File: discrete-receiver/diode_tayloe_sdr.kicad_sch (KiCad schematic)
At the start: 9 parts, among them J5 Display Connector, X1 YC24.576MUBCE2O

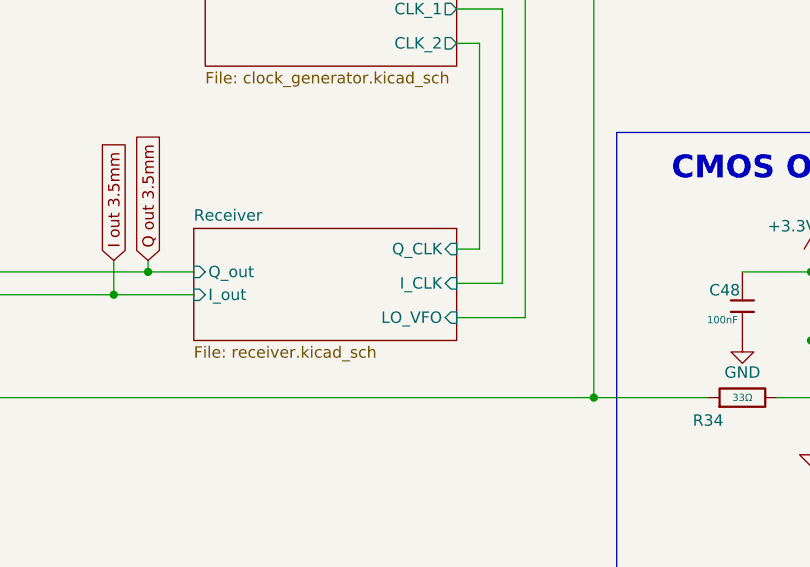
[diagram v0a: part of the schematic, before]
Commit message: Modified I, Q, and IF_LO clock order from si5351
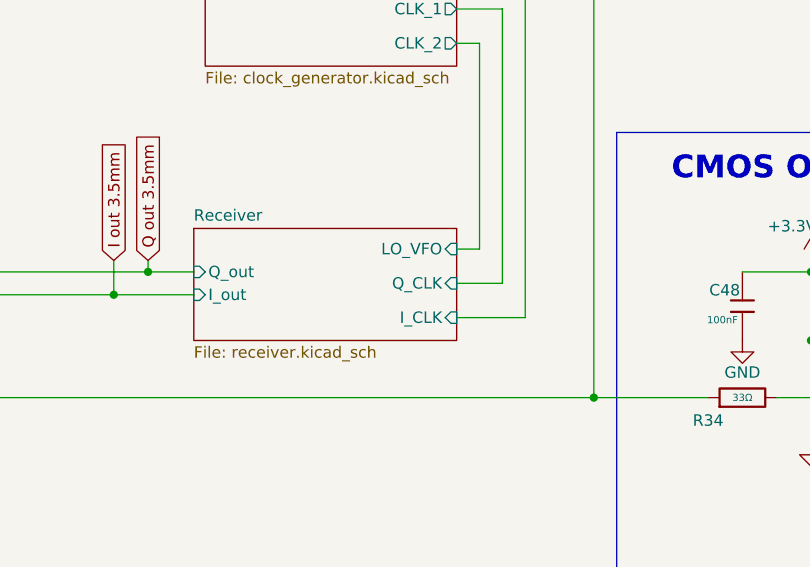
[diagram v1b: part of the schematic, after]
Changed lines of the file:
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@@
 	(wire
 		(pts
-			(xy 224.79 132.08) (xy 219.71 132.08)
+			(xy 222.25 105.41) (xy 222.25 128.27)
 		)
 		(stroke
@@
 	(wire
 		(pts
-			(xy 166.37 133.35) (xy 181.61 133.35)
+			(xy 224.79 132.08) (xy 219.71 132.08)
 		)
 		(stroke
@@
 	(wire
 		(pts
-			(xy 45.72 53.34) (xy 45.72 54.61)
+			(xy 166.37 133.35) (xy 181.61 133.35)
 		)
 		(stroke
@@
 	(wire
 		(pts
-			(xy 120.65 54.61) (xy 133.35 54.61)
+			(xy 45.72 53.34) (xy 45.72 54.61)
 		)
 		(stroke
@@
 	(wire
 		(pts
-			(xy 227.33 135.89) (xy 219.71 135.89)
+			(xy 120.65 54.61) (xy 133.35 54.61)
 		)
 		(stroke
@@
 	(wire
 		(pts
-			(xy 224.79 101.6) (xy 224.79 132.08)
-		)
-		(stroke
-			(width 0)
-			(type default)
-		)
-	)
-	(wire
-		(pts
 			(xy 259.08 130.81) (xy 259.08 138.43)
 		)
@@
 	(wire
 		(pts
-			(xy 222.25 128.27) (xy 219.71 128.27)
+			(xy 227.33 97.79) (xy 227.33 135.89)
 		)
 		(stroke
@@
 	(wire
 		(pts
-			(xy 227.33 97.79) (xy 227.33 135.89)
+			(xy 45.72 46.99) (xy 45.72 48.26)
 		)
 		(stroke
@@
 	(wire
 		(pts
-			(xy 45.72 46.99) (xy 45.72 48.26)
+			(xy 120.65 57.15) (xy 133.35 57.15)
 		)
 		(stroke
@@
 	(wire
 		(pts
-			(xy 120.65 57.15) (xy 133.35 57.15)
+			(xy 274.32 138.43) (xy 259.08 138.43)
 		)
 		(stroke
@@
 	(wire
 		(pts
-			(xy 274.32 138.43) (xy 259.08 138.43)
+			(xy 259.08 148.59) (xy 259.08 149.86)
 		)
 		(stroke
@@
 	(wire
 		(pts
-			(xy 259.08 148.59) (xy 259.08 149.86)
+			(xy 33.02 96.52) (xy 34.29 96.52)
 		)
 		(stroke
@@
 	(wire
 		(pts
-			(xy 33.02 96.52) (xy 34.29 96.52)
+			(xy 123.19 105.41) (xy 123.19 137.16)
 		)
 		(stroke
@@
 	(wire
 		(pts
-			(xy 123.19 105.41) (xy 123.19 137.16)
+			(xy 227.33 135.89) (xy 219.71 135.89)
 		)
 		(stroke
@@
 	(wire
 		(pts
-			(xy 166.37 130.81) (xy 185.42 130.81)
+			(xy 224.79 101.6) (xy 224.79 132.08)
 		)
 		(stroke
@@
 	(wire
 		(pts
-			(xy 33.02 69.85) (xy 33.02 72.39)
+			(xy 166.37 130.81) (xy 185.42 130.81)
 		)
 		(stroke
@@
 	(wire
 		(pts
-			(xy 222.25 105.41) (xy 222.25 128.27)
+			(xy 33.02 69.85) (xy 33.02 72.39)
 		)
 		(stroke
@@
 	(wire
 		(pts
+			(xy 222.25 128.27) (xy 219.71 128.27)
+		)
+		(stroke
+			(width 0)
+			(type default)
+		)
+	)
+	(wire
+		(pts
 			(xy 219.71 91.44) (xy 234.95 91.44)
 		)
@@
 		)
 		(pin "I_CLK" input
-			(at 219.71 132.08 0)
+			(at 219.71 135.89 0)
 			(effects
 				(font
@@
 		)
 		(pin "LO_VFO" input
-			(at 219.71 135.89 0)
+			(at 219.71 128.27 0)
 			(effects
 				(font
@@
 		)
 		(pin "Q_CLK" input
-			(at 219.71 128.27 0)
+			(at 219.71 132.08 0)
 			(effects
 				(font

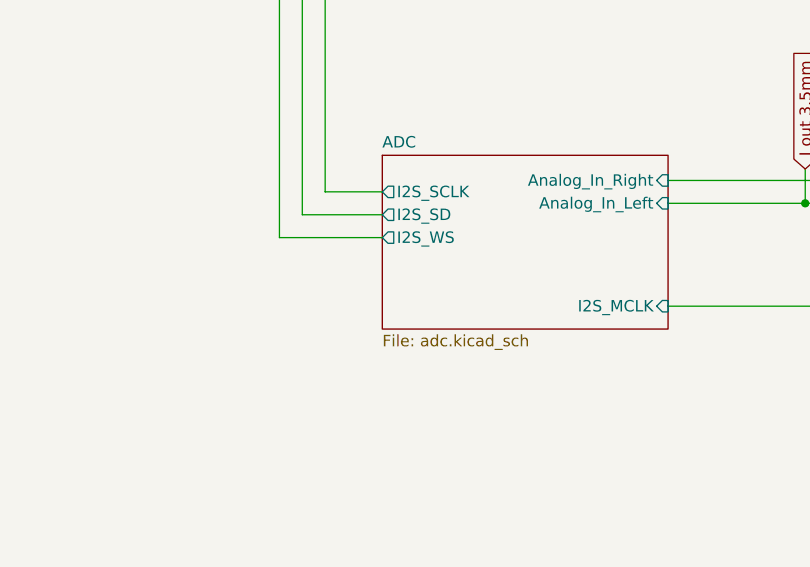
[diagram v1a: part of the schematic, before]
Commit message: Added ADC mode GPIO connections, and changed second red LED to green
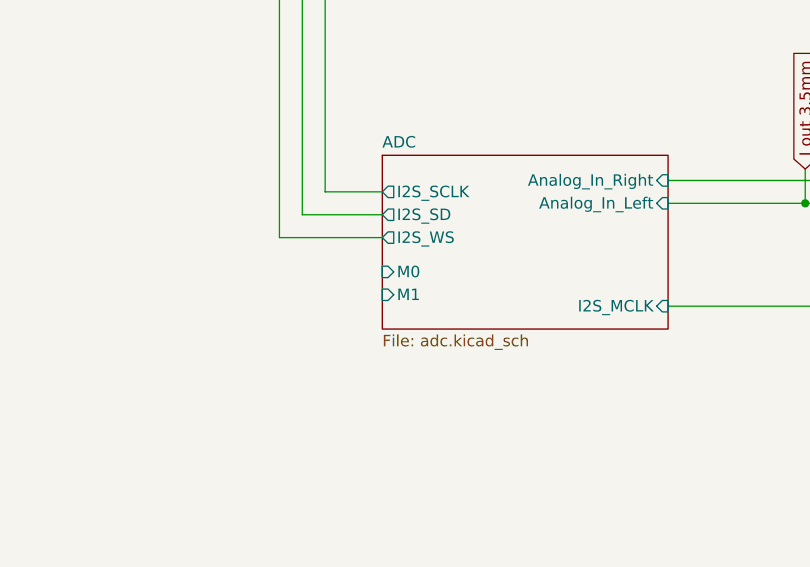
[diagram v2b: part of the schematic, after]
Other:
- sheet ADC ports: added M0, M1; removed none
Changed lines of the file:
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@@
+			)
+		)
+		(pin "M0" input
+			(at 134.62 140.97 180)
+			(effects
+				(font
+					(size 1.27 1.27)
+				)
+				(justify left)
+			)
+		)
+		(pin "M1" input
+			(at 134.62 143.51 180)
+			(effects
+				(font
+					(size 1.27 1.27)
+				)
+				(justify left)
 			)
 		)

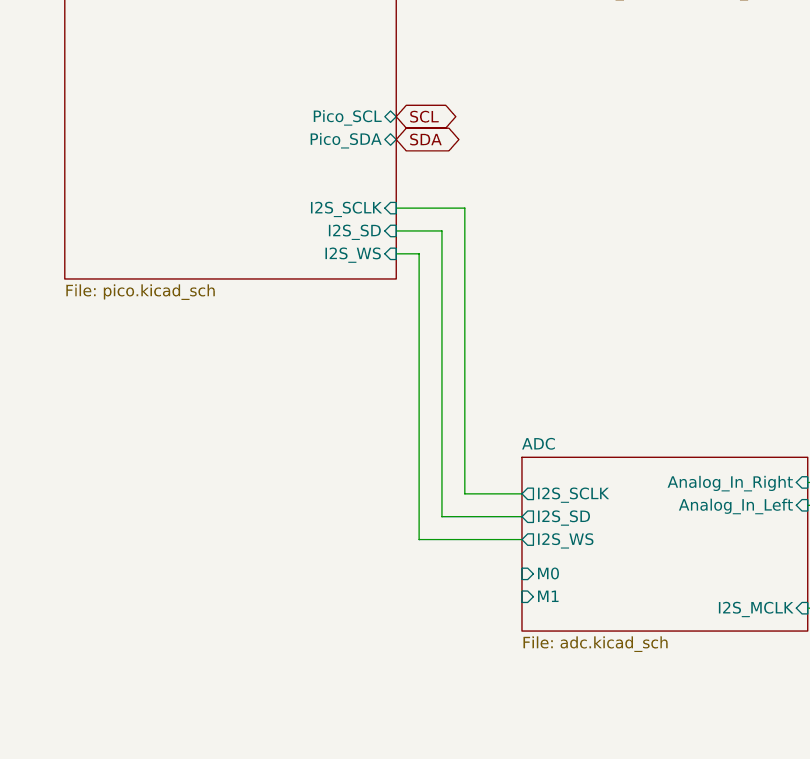
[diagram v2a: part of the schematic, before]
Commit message: Finished connecting ADC M0, M1, started PCB edge cut design
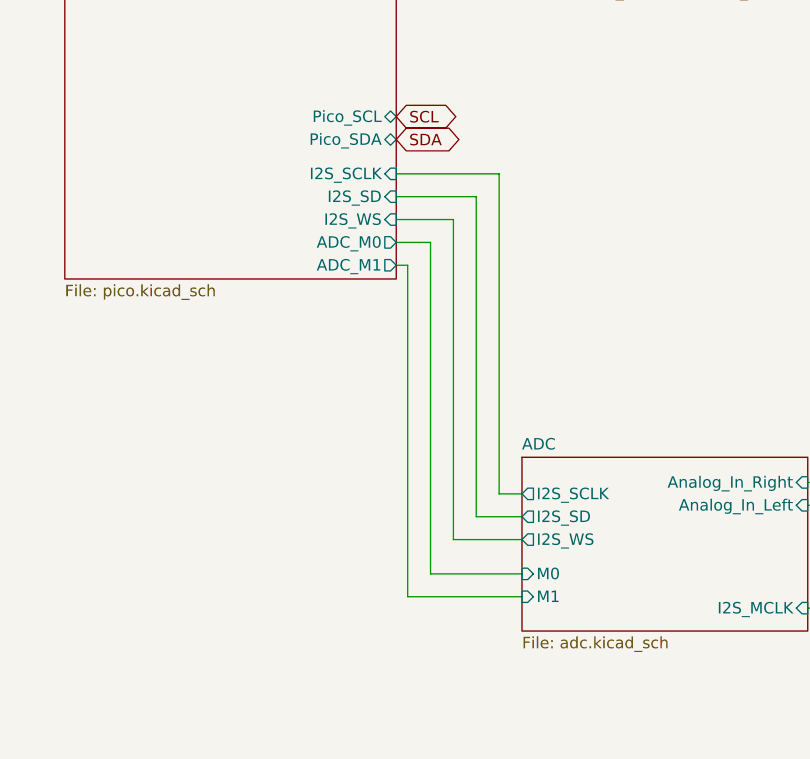
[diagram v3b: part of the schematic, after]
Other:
- sheet Pico ports: added ADC_M0, ADC_M1; removed none
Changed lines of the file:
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@@
 	(wire
 		(pts
+			(xy 120.65 104.14) (xy 124.46 104.14)
+		)
+		(stroke
+			(width 0)
+			(type default)
+		)
+	)
+	(wire
+		(pts
 			(xy 120.65 62.23) (xy 133.35 62.23)
 		)
@@
 	(wire
 		(pts
+			(xy 124.46 140.97) (xy 134.62 140.97)
+		)
+		(stroke
+			(width 0)
+			(type default)
+		)
+	)
+	(wire
+		(pts
 			(xy 166.37 133.35) (xy 181.61 133.35)
 		)
@@
 	(wire
 		(pts
-			(xy 123.19 137.16) (xy 134.62 137.16)
+			(xy 121.92 143.51) (xy 121.92 106.68)
+		)
+		(stroke
+			(width 0)
+			(type default)
+		)
+	)
+	(wire
+		(pts
+			(xy 127 137.16) (xy 134.62 137.16)
 		)
 		(stroke
@@
 	(wire
 		(pts
-			(xy 120.65 105.41) (xy 123.19 105.41)
+			(xy 120.65 101.6) (xy 127 101.6)
 		)
 		(stroke
@@
 	(wire
 		(pts
+			(xy 124.46 104.14) (xy 124.46 140.97)
+		)
+		(stroke
+			(width 0)
+			(type default)
+		)
+	)
+	(wire
+		(pts
 			(xy 55.88 39.37) (xy 59.69 39.37)
 		)
@@
 	(wire
 		(pts
+			(xy 121.92 106.68) (xy 120.65 106.68)
+		)
+		(stroke
+			(width 0)
+			(type default)
+		)
+	)
+	(wire
+		(pts
+			(xy 134.62 143.51) (xy 121.92 143.51)
+		)
+		(stroke
+			(width 0)
+			(type default)
+		)
+	)
+	(wire
+		(pts
 			(xy 259.08 138.43) (xy 259.08 140.97)
 		)
@@
 	(wire
 		(pts
-			(xy 123.19 105.41) (xy 123.19 137.16)
+			(xy 127 101.6) (xy 127 137.16)
 		)
 		(stroke
@@
 	(wire
 		(pts
-			(xy 120.65 100.33) (xy 128.27 100.33)
+			(xy 120.65 96.52) (xy 132.08 96.52)
 		)
 		(stroke
@@
 	(wire
 		(pts
-			(xy 125.73 134.62) (xy 134.62 134.62)
+			(xy 129.54 134.62) (xy 134.62 134.62)
 		)
 		(stroke
@@
 	(wire
 		(pts
-			(xy 128.27 132.08) (xy 134.62 132.08)
+			(xy 132.08 132.08) (xy 134.62 132.08)
 		)
 		(stroke
@@
 	(wire
 		(pts
-			(xy 125.73 102.87) (xy 125.73 134.62)
+			(xy 129.54 99.06) (xy 129.54 134.62)
 		)
 		(stroke
@@
 	(wire
 		(pts
-			(xy 128.27 100.33) (xy 128.27 132.08)
+			(xy 132.08 96.52) (xy 132.08 132.08)
 		)
 		(stroke
@@
 	(wire
 		(pts
-			(xy 120.65 102.87) (xy 125.73 102.87)
+			(xy 120.65 99.06) (xy 129.54 99.06)
 		)
 		(stroke
@@
 		)
 		(pin "I2S_SCLK" input
-			(at 120.65 100.33 0)
+			(at 120.65 96.52 0)
 			(effects
 				(font
@@
 		)
 		(pin "I2S_SD" input
-			(at 120.65 102.87 0)
+			(at 120.65 99.06 0)
 			(effects
 				(font
@@
 		)
 		(pin "I2S_WS" input
-			(at 120.65 105.41 0)
+			(at 120.65 101.6 0)
 			(effects
 				(font
@@
 			(effects
 				(font
+					(size 1.27 1.27)
+				)
+				(justify right)
+			)
+		)
+		(pin "ADC_M0" output
+			(at 120.65 104.14 0)
+			(effects
+				(font
+					(size 1.27 1.27)
+				)
+				(justify right)
+			)
+		)
+		(pin "ADC_M1" output
+			(at 120.65 106.68 0)
+			(effects
+				(font

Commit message: Made ERC progress
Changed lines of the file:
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@@
 	)
 	(junction
-		(at 45.72 53.34)
+		(at 181.61 133.35)
 		(diameter 0)
 		(color 0 0 0 0)
 	)
 	(junction
-		(at 55.88 39.37)
+		(at 45.72 53.34)
 		(diameter 0)
 		(color 0 0 0 0)
 	)
 	(junction
-		(at 33.02 72.39)
+		(at 55.88 39.37)
 		(diameter 0)
 		(color 0 0 0 0)
 	)
 	(junction
-		(at 234.95 144.78)
+		(at 33.02 72.39)
 		(diameter 0)
 		(color 0 0 0 0)
@@
 	)
 	(junction
-		(at 45.72 48.26)
+		(at 234.95 144.78)
 		(diameter 0)
 		(color 0 0 0 0)
 	)
 	(junction
-		(at 185.42 130.81)
+		(at 45.72 48.26)
 		(diameter 0)
 		(color 0 0 0 0)
 	)
 	(junction
-		(at 181.61 133.35)
+		(at 259.08 130.81)
 		(diameter 0)
 		(color 0 0 0 0)
 	)
 	(junction
-		(at 259.08 130.81)
+		(at 185.42 130.81)
 		(diameter 0)
 		(color 0 0 0 0)
@@
 	(wire
 		(pts
-			(xy 120.65 104.14) (xy 124.46 104.14)
+			(xy 120.65 104.14) (xy 128.27 104.14)
 		)
 		(stroke
@@
 	(wire
 		(pts
-			(xy 124.46 140.97) (xy 134.62 140.97)
+			(xy 128.27 140.97) (xy 142.24 140.97)
 		)
 		(stroke
@@
 	(wire
 		(pts
-			(xy 166.37 133.35) (xy 181.61 133.35)
+			(xy 173.99 133.35) (xy 181.61 133.35)
 		)
 		(stroke
@@
 	(wire
 		(pts
-			(xy 121.92 143.51) (xy 121.92 106.68)
+			(xy 125.73 143.51) (xy 125.73 106.68)
 		)
 		(stroke
@@
 	(wire
 		(pts
-			(xy 127 137.16) (xy 134.62 137.16)
+			(xy 130.81 137.16) (xy 142.24 137.16)
 		)
 		(stroke
@@
 	(wire
 		(pts
-			(xy 120.65 101.6) (xy 127 101.6)
+			(xy 120.65 101.6) (xy 130.81 101.6)
 		)
 		(stroke
@@
 	(wire
 		(pts
-			(xy 124.46 104.14) (xy 124.46 140.97)
+			(xy 128.27 104.14) (xy 128.27 140.97)
 		)
 		(stroke
@@
 	(wire
 		(pts
-			(xy 121.92 106.68) (xy 120.65 106.68)
+			(xy 125.73 106.68) (xy 120.65 106.68)
 		)
 		(stroke
@@
 	(wire
 		(pts
-			(xy 134.62 143.51) (xy 121.92 143.51)
+			(xy 142.24 143.51) (xy 125.73 143.51)
 		)
 		(stroke
@@
 	(wire
 		(pts
-			(xy 127 101.6) (xy 127 137.16)
+			(xy 130.81 101.6) (xy 130.81 137.16)
 		)
 		(stroke
@@
 	(wire
 		(pts
-			(xy 120.65 96.52) (xy 132.08 96.52)
+			(xy 120.65 96.52) (xy 135.89 96.52)
 		)
 		(stroke
@@
 	(wire
 		(pts
-			(xy 129.54 134.62) (xy 134.62 134.62)
+			(xy 133.35 134.62) (xy 142.24 134.62)
 		)
 		(stroke
@@
 	(wire
 		(pts
-			(xy 166.37 144.78) (xy 234.95 144.78)
+			(xy 173.99 144.78) (xy 234.95 144.78)
 		)
 		(stroke
@@
 	(wire
 		(pts
-			(xy 166.37 130.81) (xy 185.42 130.81)
+			(xy 173.99 130.81) (xy 185.42 130.81)
 		)
 		(stroke
@@
 	(wire
 		(pts
-			(xy 132.08 132.08) (xy 134.62 132.08)
+			(xy 135.89 132.08) (xy 142.24 132.08)
 		)
 		(stroke
@@
 	(wire
 		(pts
-			(xy 129.54 99.06) (xy 129.54 134.62)
+			(xy 133.35 99.06) (xy 133.35 134.62)
 		)
 		(stroke
@@
 	(wire
 		(pts
-			(xy 132.08 96.52) (xy 132.08 132.08)
+			(xy 135.89 96.52) (xy 135.89 132.08)
 		)
 		(stroke
@@
 	(wire
 		(pts
-			(xy 120.65 99.06) (xy 129.54 99.06)
+			(xy 120.65 99.06) (xy 133.35 99.06)
 		)
 		(stroke
@@
 	)
 	(sheet
-		(at 134.62 128.016)
+		(at 142.24 128.016)
 		(size 31.75 19.304)
 		(exclude_from_sim no)
@@
 		)
 		(property "Sheetname" "ADC"
-			(at 134.62 127.3044 0)
+			(at 142.24 127.3044 0)
 			(show_name no)
 			(do_not_autoplace no)
@@
 		)
 		(property "Sheetfile" "adc.kicad_sch"
-			(at 134.62 147.9046 0)
+			(at 142.24 147.9046 0)
 			(show_name no)
 			(do_not_autoplace no)
@@
 		)
 		(pin "Analog_In_Left" input
-			(at 166.37 133.35 0)
+			(at 173.99 133.35 0)
 			(effects
 				(font
@@
 		)
 		(pin "Analog_In_Right" input
-			(at 166.37 130.81 0)
+			(at 173.99 130.81 0)
 			(effects
 				(font
@@
 		)
 		(pin "I2S_MCLK" input
-			(at 166.37 144.78 0)
+			(at 173.99 144.78 0)
 			(effects
 				(font
@@
 		)
 		(pin "I2S_SCLK" output
-			(at 134.62 132.08 180)
+			(at 142.24 132.08 180)
 			(effects
 				(font
@@
 		)
 		(pin "I2S_SD" output
-			(at 134.62 134.62 180)
+			(at 142.24 134.62 180)
 			(effects
 				(font
@@
 		)
 		(pin "I2S_WS" output
-			(at 134.62 137.16 180)
+			(at 142.24 137.16 180)
 			(effects
 				(font
@@
 		)
 		(pin "M0" input
-			(at 134.62 140.97 180)
+			(at 142.24 140.97 180)
 			(effects
 				(font
@@
 		)
 		(pin "M1" input
-			(at 134.62 143.51 180)
+			(at 142.24 143.51 180)
 			(effects
 				(font

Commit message: PCB edge cuts finalized
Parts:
- added H1, H2, H3, H4: MountingHole, MountingHole:MountingHole_3.2mm_M3, symbol Mechanical:MountingHole

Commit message: PCB Progress
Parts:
- added D1: Red, PCM_JLCPCB:D_0603, symbol PCM_JLCPCB-Diodes:LED,0603,Red
- added R7: 1kΩ, PCM_JLCPCB:R_0402, symbol PCM_JLCPCB-Resistors:0402,1kΩ
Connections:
- net GND: now also R7.2
- new net: D1.1, R7.1
- new net +5V: D1.2
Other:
- note added: "Power LED"

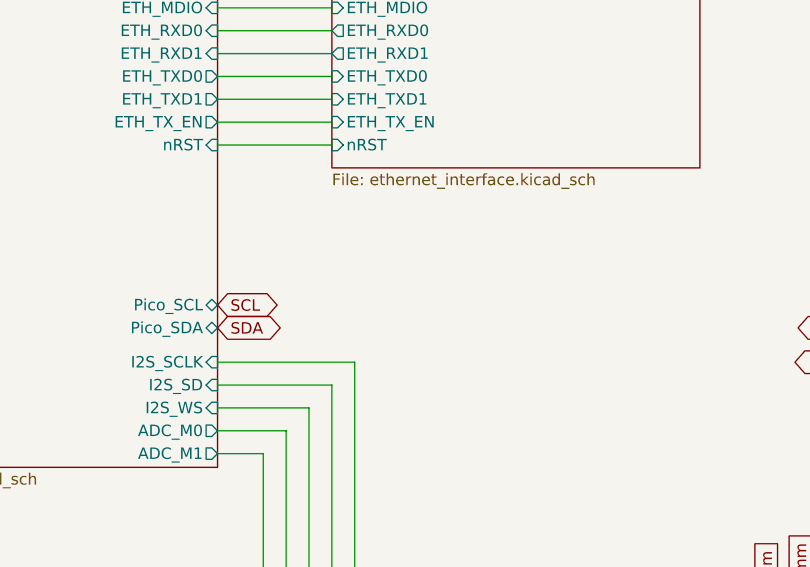
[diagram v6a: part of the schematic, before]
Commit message: Added test pads for SDA and SCL
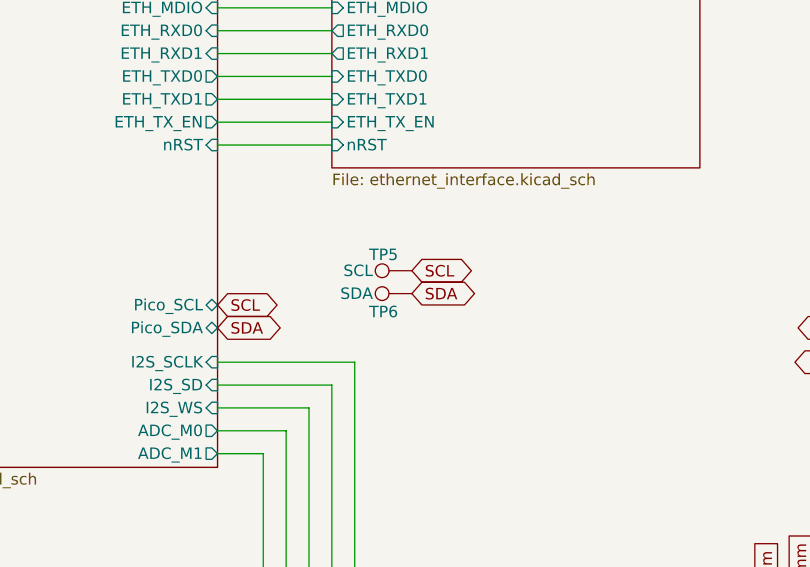
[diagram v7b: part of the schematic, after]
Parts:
- added TP5: SCL, TestPoint:TestPoint_Pad_1.5x1.5mm, symbol Connector:TestPoint
- added TP6: SDA, TestPoint:TestPoint_Pad_1.5x1.5mm, symbol Connector:TestPoint
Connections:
- net SCL: now also TP5.1
- net SDA: now also TP6.1
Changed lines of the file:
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@@
+		)
+	)
+	(global_label "SDA"
+		(shape bidirectional)
+		(at 142.24 88.9 0)
+		(fields_autoplaced yes)
+		(effects
+			(font
+				(size 1.27 1.27)
+				(thickness 0.1588)
+			)
+			(justify left)
+		)
+		(property "Intersheetrefs" "${INTERSHEET_REFS}"
+			(at 149.9046 88.9 0)
+			(hide yes)
+			(show_name no)
+			(do_not_autoplace no)
+			(effects
+				(font
+					(size 1.27 1.27)
+				)
+				(justify left)
+			)
 		)
 	)
@@
 				)
 				(justify right)
+			)
+		)
+	)
+	(global_label "SCL"
+		(shape bidirectional)
+		(at 142.24 86.36 0)
+		(fields_autoplaced yes)
+		(effects
+			(font
+				(size 1.27 1.27)
+				(thickness 0.1588)
+			)
+			(justify left)
+		)
+		(property "Intersheetrefs" "${INTERSHEET_REFS}"
+			(at 149.8441 86.36 0)
+			(hide yes)
+			(show_name no)
+			(do_not_autoplace no)
+			(effects
+				(font
+					(size 1.27 1.27)
+				)
+				(justify left)
 			)
 		)
@@
 	)
 	(symbol
+		(lib_id "Connector:TestPoint")
+		(at 142.24 86.36 90)
+		(unit 1)
+		(body_style 1)
+		(exclude_from_sim no)
+		(in_bom yes)
+		(on_board yes)
+		(in_pos_files yes)
+		(dnp no)
+		(property "Reference" "TP5"
+			(at 140.716 84.582 90)
+			(show_name no)
+			(do_not_autoplace no)
+			(effects
+				(font
+					(size 1.27 1.27)
+				)
+				(justify left)
+			)
+		)
+		(property "Value" "SCL"
+			(at 137.922 86.36 90)
+			(show_name no)
+			(do_not_autoplace no)
+			(effects
+				(font
+					(size 1.27 1.27)
+				)
+				(justify left)
+			)
+		)
+		(property "Footprint" "TestPoint:TestPoint_Pad_1.5x1.5mm"
+			(at 142.24 81.28 0)
+			(hide yes)
+			(show_name no)
+			(do_not_autoplace no)
+			(effects
+				(font
+					(size 1.27 1.27)
+				)
+			)
+		)
+		(property "Datasheet" ""
+			(at 142.24 81.28 0)
+			(hide yes)
+			(show_name no)
+			(do_not_autoplace no)
+			(effects
+				(font
+					(size 1.27 1.27)
+				)
+			)
+		)
+		(property "Description" "test point"
+			(at 142.24 86.36 0)
+			(hide yes)
+			(show_name no)
+			(do_not_autoplace no)
+			(effects
+				(font
+					(size 1.27 1.27)
+				)
+			)
+		)
+		(pin "1"
+		)
+		(instances
+			(project "diode_tayloe_sdr"
+				(path "/d18d178d-3f10-4d68-9036-eae71a7d091a"
+					(reference "TP5")
+					(unit 1)
+				)
+			)
+		)
+	)
+	(symbol
 		(lib_id "power:+3.3V")
 		(at 259.08 129.54 0)
@@
 					(unit 1)
 				)
+			)
+		)
+	)
+	(symbol
+		(lib_id "Connector:TestPoint")
+		(at 142.24 88.9 90)
+		(unit 1)
+		(body_style 1)
+		(exclude_from_sim no)
+		(in_bom yes)
+		(on_board yes)
+		(in_pos_files yes)
+		(dnp no)
+		(property "Reference" "TP6"
+			(at 140.716 90.932 90)
+			(show_name no)
+			(do_not_autoplace no)
+			(effects
+				(font
+					(size 1.27 1.27)
+				)
+				(justify left)
+			)
+		)
+		(property "Value" "SDA"
+			(at 137.922 88.9 90)
+			(show_name no)
+			(do_not_autoplace no)
+			(effects
+				(font
+					(size 1.27 1.27)
+				)
+				(justify left)
+			)
+		)
+		(property "Footprint" "TestPoint:TestPoint_Pad_1.5x1.5mm"
+			(at 142.24 83.82 0)
+			(hide yes)
+			(show_name no)
+			(do_not_autoplace no)
+			(effects
+				(font
+					(size 1.27 1.27)
+				)
+			)
+		)
+		(property "Datasheet" ""
+			(at 142.24 83.82 0)
+			(hide yes)
+			(show_name no)
+			(do_not_autoplace no)
+			(effects
+				(font
+					(size 1.27 1.27)
+				)
+			)
+		)
+		(property "Description" "test point"
+			(at 142.24 88.9 0)
+			(hide yes)
+			(show_name no)
+			(do_not_autoplace no)
+			(effects
+				(font
+					(size 1.27 1.27)
+				)
+			)
+		)
+		(pin "1"
+		)
+		(instances
+			(project "diode_tayloe_sdr"
+				(path "/d18d178d-3f10-4d68-9036-eae71a7d091a"
+					(reference "TP6")
+					(unit 1)
+				)
